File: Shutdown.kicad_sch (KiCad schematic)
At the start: 13 parts, among them K1 EX12U1S, Q12 2N7002NXAKR, Q13 NTR5105PT1G, Q14 2N7002NXAKR

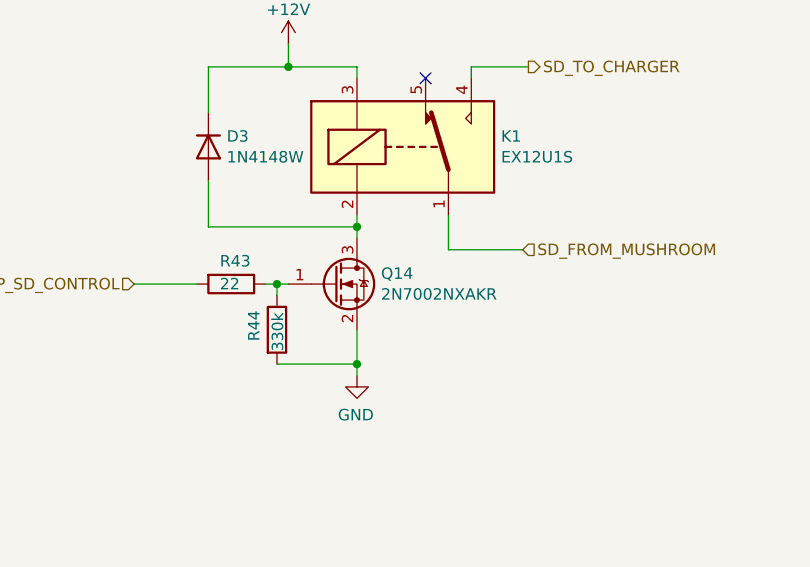
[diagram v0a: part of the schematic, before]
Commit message: Changed mosfet, fixed all the datasheets, added 3D models
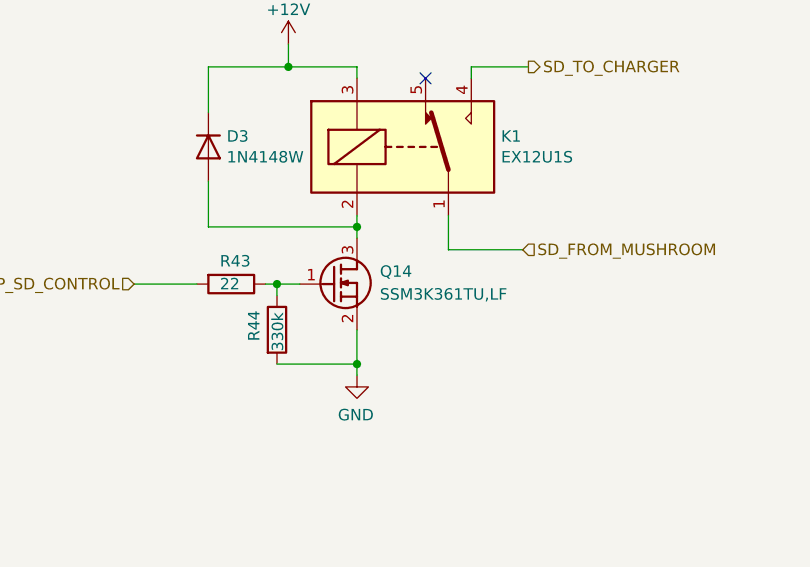
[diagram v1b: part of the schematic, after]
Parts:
- removed Q14: 2N7002NXAKR, Package_TO_SOT_SMD:SOT-23, symbol Transistor_FET:2N7002
- added Q14: SSM3K361TU,LF, 00_proj-lib:SOTFL65P210X75-3N, symbol 00_proj-lib:SSM3K361TU,LF
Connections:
- net GND: now also Q14.2 (S)
- net at D3.2 (A), K1.2: now also Q14.3 (D)
- net at R43.1, R44.1: now also Q14.1 (G)
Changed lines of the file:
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@@
     (stroke (width 0) (type default) (color 0 0 0 0))
   )
-  (wire (pts (xy 201.93 91.44) (xy 203.2 91.44))
+  (wire (pts (xy 201.93 91.44) (xy 204.47 91.44))
     (stroke (width 0) (type default) (color 0 0 0 0))
   )
@@
       (effects (font (size 1.27 1.27)) hide)
     )
-    (property "Datasheet" "~" (id 3) (at 204.47 130.175 0)
+    (property "Datasheet" "datasheets\\rgl34a-1768034.pdf" (id 3) (at 204.47 130.175 0)
       (effects (font (size 1.27 1.27)) hide)
     )
@@
       (effects (font (size 1.27 1.27)) hide)
     )
-    (property "Datasheet" "https://www.mouser.it/datasheet/2/212/1/relay_ex1_ex2_e-844962.pdf" (id 3) (at 215.9 76.2 0)
+    (property "Datasheet" "datasheets/relay_ex1_ex2_e-844962.pdf" (id 3) (at 215.9 76.2 0)
       (effects (font (size 1.27 1.27)) hide)
     )
@@
     (pin "1")
   )
+  (symbol (lib_id "00_proj-lib:SSM3K361TU,LF") (at 203.2 93.345 0) (unit 1)
+    (in_bom yes) (on_board yes) (fields_autoplaced)
+    (property "Reference" "Q14" (id 0) (at 213.36 90.0429 0)
+      (effects (font (size 1.27 1.27)) (justify left))
+    )
+    (property "Value" "SSM3K361TU,LF" (id 1) (at 213.36 92.5829 0)
+      (effects (font (size 1.27 1.27)) (justify left))
+    )
+    (property "Footprint" "00_proj-lib:SOTFL65P210X75-3N" (id 2) (at 203.2 93.345 0)
+      (effects (font (size 1.27 1.27)) hide)
+    )
+    (property "Datasheet" "datasheets\\SSM3K361TU.pdf" (id 3) (at 203.2 93.345 0)
+      (effects (font (size 1.27 1.27)) hide)
+    )
+    (property "Height" "0.75" (id 8) (at 214.63 492.075 0)
+      (effects (font (size 1.27 1.27)) (justify left top) hide)
+    )
+    (property "Mouser Part Number" "757-SSM3K361TULF" (id 9) (at 214.63 592.075 0)
+      (effects (font (size 1.27 1.27)) (justify left top) hide)
+    )
+    (property "Mouser Price/Stock" "https://www.mouser.co.uk/ProductDetail/Toshiba/SSM3K361TULF?qs=r5DSvlrkXmLO9ymRQhnt0A%3D%3D" (id 10) (at 214.63 692.075 0)
+      (effects (font (size 1.27 1.27)) (justify left top) hide)
+    )
+    (property "Manufacturer_Name" "Toshiba" (id 11) (at 214.63 792.075 0)
+      (effects (font (size 1.27 1.27)) (justify left top) hide)
+    )
+    (property "Manufacturer_Part_Number" "SSM3K361TU,LF" (id 12) (at 214.63 892.075 0)
+      (effects (font (size 1.27 1.27)) (justify left top) hide)
+    )
+    (pin "1")
+    (pin "2")
+    (pin "3")
+  )
   (symbol (lib_id "Device:R") (at 196.85 91.44 270) (unit 1)
     (in_bom yes) (on_board yes)
@@
     (pin "1")
   )
-  (symbol (lib_id "Transistor_FET:2N7002") (at 208.28 91.44 0) (unit 1)
-    (in_bom yes) (on_board yes)
-    (property "Reference" "Q14" (id 0) (at 213.487 90.2716 0)
-      (effects (font (size 1.27 1.27)) (justify left))
-    )
-    (property "Value" "2N7002NXAKR" (id 1) (at 213.487 92.583 0)
-      (effects (font (size 1.27 1.27)) (justify left))
-    )
-    (property "Footprint" "Package_TO_SOT_SMD:SOT-23" (id 2) (at 213.36 93.345 0)
-      (effects (font (size 1.27 1.27) italic) (justify left) hide)
-    )
-    (property "Datasheet" "https://www.onsemi.com/pub/Collateral/NDS7002A-D.PDF" (id 3) (at 208.28 91.44 0)
-      (effects (font (size 1.27 1.27)) (justify left) hide)
-    )
-    (pin "1")
-    (pin "2")
-    (pin "3")
-  )
   (symbol (lib_id "Transistor_FET:2N7002") (at 69.215 104.14 0) (unit 1)
     (in_bom yes) (on_board yes)
@@
       (effects (font (size 1.27 1.27) italic) (justify left) hide)
     )
-    (property "Datasheet" "https://www.onsemi.com/pub/Collateral/NDS7002A-D.PDF" (id 3) (at 69.215 104.14 0)
+    (property "Datasheet" "datasheets/NDS7002A-D.pdf" (id 3) (at 69.215 104.14 0)
       (effects (font (size 1.27 1.27)) (justify left) hide)
     )
@@
       (effects (font (size 1.27 1.27)) hide)
     )
-    (property "Datasheet" "~" (id 3) (at 86.995 95.25 0)
+    (property "Datasheet" "datasheets/NTR5105P_D-2319014.pdf" (id 3) (at 86.995 95.25 0)
       (effects (font (size 1.27 1.27)) hide)
     )
@@
       (effects (font (size 1.27 1.27)) hide)
     )
-    (property "Datasheet" "~" (id 3) (at 199.39 137.16 0)
-      (effects (font (size 1.27 1.27)) hide)
-    )
+    (property "Datasheet" "datasheets/DIOD-S-A0002238313-1.pdf" (id 3) (at 199.39 137.16 0)
+      (effects (font (size 1.27 1.27)) hide)
+    )
